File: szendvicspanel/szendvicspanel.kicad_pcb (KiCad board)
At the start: 2 copper layers, 23 parts, among them Q3 BS170, Q4 BS170, Q5 BS250, Q6 BS250, Q7 BS170, Q8 BS170, U1 TL072, U2 TL072

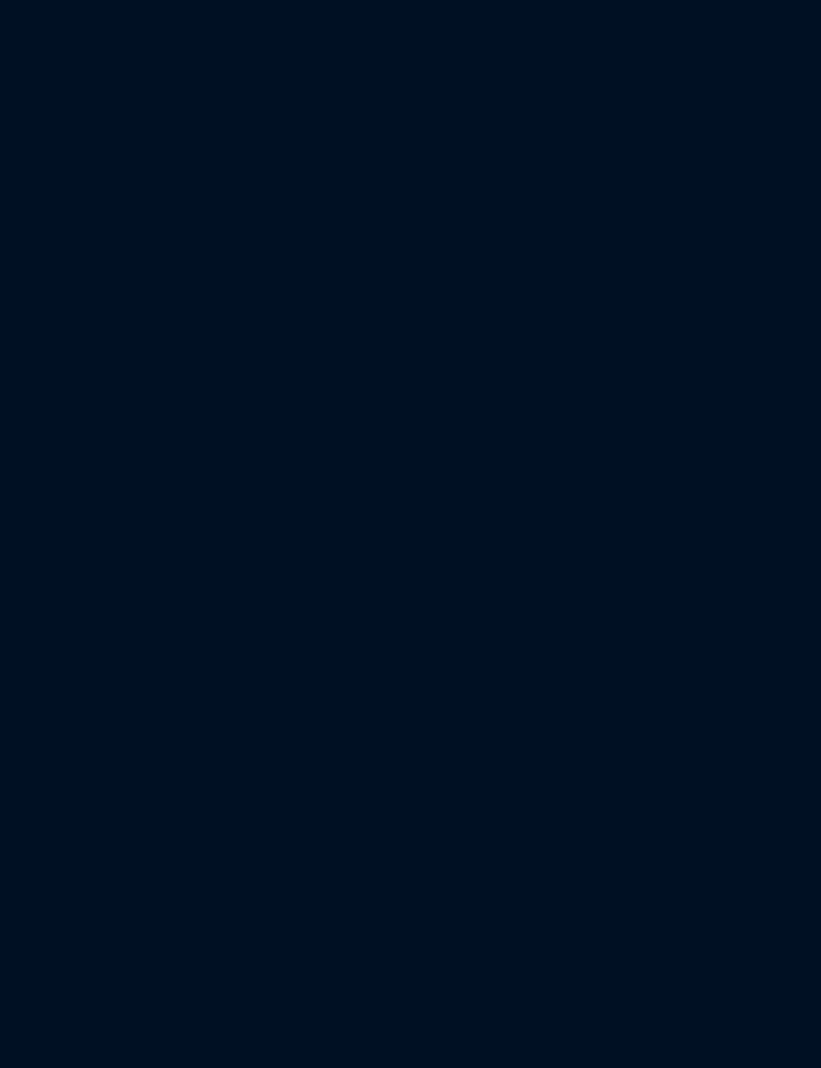
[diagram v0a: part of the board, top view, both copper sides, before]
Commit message: Jelgenerátor layer schematic
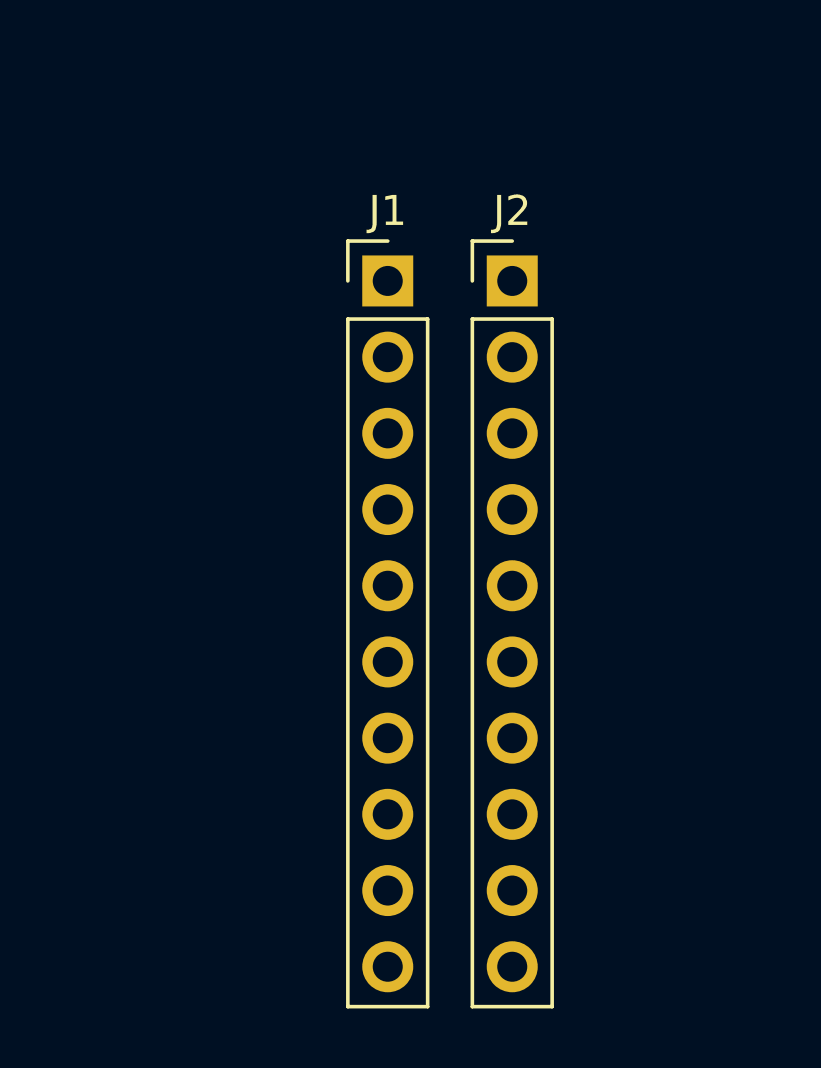
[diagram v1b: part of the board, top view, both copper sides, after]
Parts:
- added J1: Conn_01x10_Socket, Connector_PinHeader_2.54mm:PinHeader_1x10_P2.54mm_Vertical, F.Cu at (91.3, 106.6)
- added J2: Conn_01x10_Socket, Connector_PinHeader_2.54mm:PinHeader_1x10_P2.54mm_Vertical, F.Cu at (95.5, 106.6)
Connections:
- net Net-(U1A-+) renamed /Jelgenerátor és analóg modul/VREF
- RV1 pad 1: GND -> /Jelgenerátor és analóg modul/GND
- RV1 pad 2: /CMOS H-híd és driver modul/input -> /Jelgenerátor és analóg modul/square_out
- RV2 pad 1: +12V -> /Jelgenerátor és analóg modul/VIN
- RV2 pad 3: GND -> /Jelgenerátor és analóg modul/GND
- U1 pad 4: GND -> /Jelgenerátor és analóg modul/GND
- U1 pad 8: +12V -> /Jelgenerátor és analóg modul/VIN
- U2 pad 4: GND -> /Jelgenerátor és analóg modul/GND
- U2 pad 8: +12V -> /Jelgenerátor és analóg modul/VIN

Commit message: Jelgenerátor layer, README, .gitignore
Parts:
- removed C1: 3,2n, Capacitor_THT:C_Axial_L3.8mm_D2.6mm_P7.50mm_Horizontal
- removed C2: 100n, Capacitor_THT:C_Axial_L3.8mm_D2.6mm_P7.50mm_Horizontal
- removed J1, J2: Conn_01x10_Socket, Connector_PinHeader_2.54mm:PinHeader_1x10_P2.54mm_Vertical
- removed LS1, LS2: Speaker_Ultrasound, Connector_PinHeader_1.27mm:PinHeader_1x02_P1.27mm_Horizontal
- removed Q3, Q4, Q7, Q8: BS170, Package_TO_SOT_THT:TO-92_Inline
- removed Q5, Q6: BS250, Package_TO_SOT_THT:TO-92_Inline
- removed R1: 2,4k, Resistor_THT:R_Axial_DIN0204_L3.6mm_D1.6mm_P5.08mm_Horizontal
- removed R10, R9: 3,3k, Resistor_THT:R_Axial_DIN0204_L3.6mm_D1.6mm_P5.08mm_Horizontal
- removed R2, R5: 1k, Resistor_THT:R_Axial_DIN0204_L3.6mm_D1.6mm_P5.08mm_Horizontal
- removed R3: 2k, Resistor_THT:R_Axial_DIN0204_L3.6mm_D1.6mm_P5.08mm_Horizontal
- removed R7, R8: 240, Resistor_THT:R_Axial_DIN0204_L3.6mm_D1.6mm_P5.08mm_Horizontal
- removed RV1, RV2, RV3: R_Potentiometer, Potentiometer_THT:Potentiometer_Vishay_T93YA_Vertical
- removed U1, U2: TL072, Package_DIP:DIP-8_W7.62mm
